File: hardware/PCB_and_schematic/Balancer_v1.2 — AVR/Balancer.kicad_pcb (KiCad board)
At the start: 2 copper layers, 99.5 x 99.5 mm, 189 parts, among them J1 BATT_OUT, J10 RS485, J11 HEATSING_TEMP1, J12 External Current Shunt, J13 BATT_IN, J2 VOLTAGE_3WIRE, J3 Conn_01x03, J4 HEATSING_TEMP1, J5 FAN1, J6 FAN2, J7 BATT_12V, J8 ICP, J9 RS485, Q1 BC817, Q10 TIP41C, Q11 TIP41C, Q12 BC807, Q13 BD238, Q14 TIP41C, Q15 BC807, Q16 BD238, Q17 BC817, Q19 BC817, Q2 BC337, Q20 BC817, Q21 BC817, Q22 BC817, Q23 TIP41C, Q3 BC327, Q4 PMOS, Q5 PMOS, Q6 BC337, Q7 BC327, Q8 BC817, Q9 BC817, U1 LM324, U2 LM324, U3 LM358, U4 TL432DBZ, U6 ST485, U7 INA226, U8 AVR64DD28

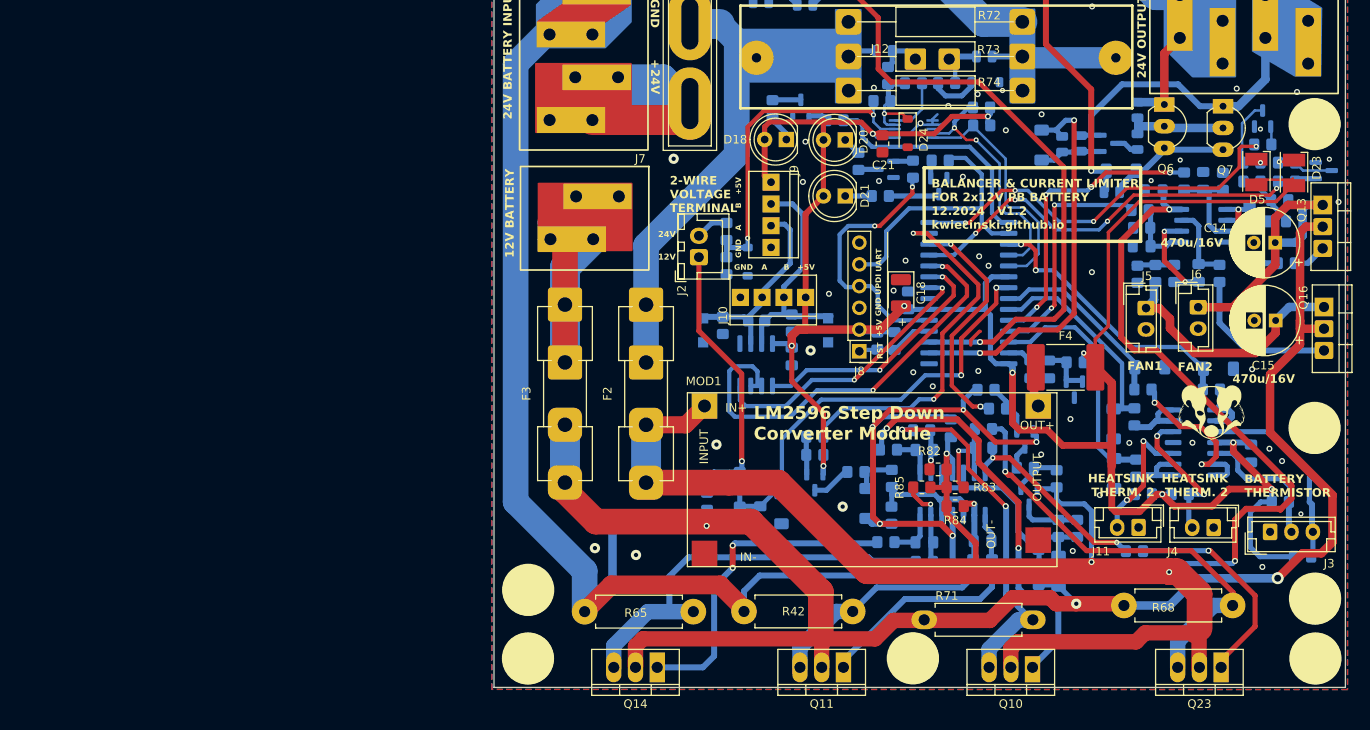
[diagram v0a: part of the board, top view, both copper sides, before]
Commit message: New version of balancer PCB and schematic
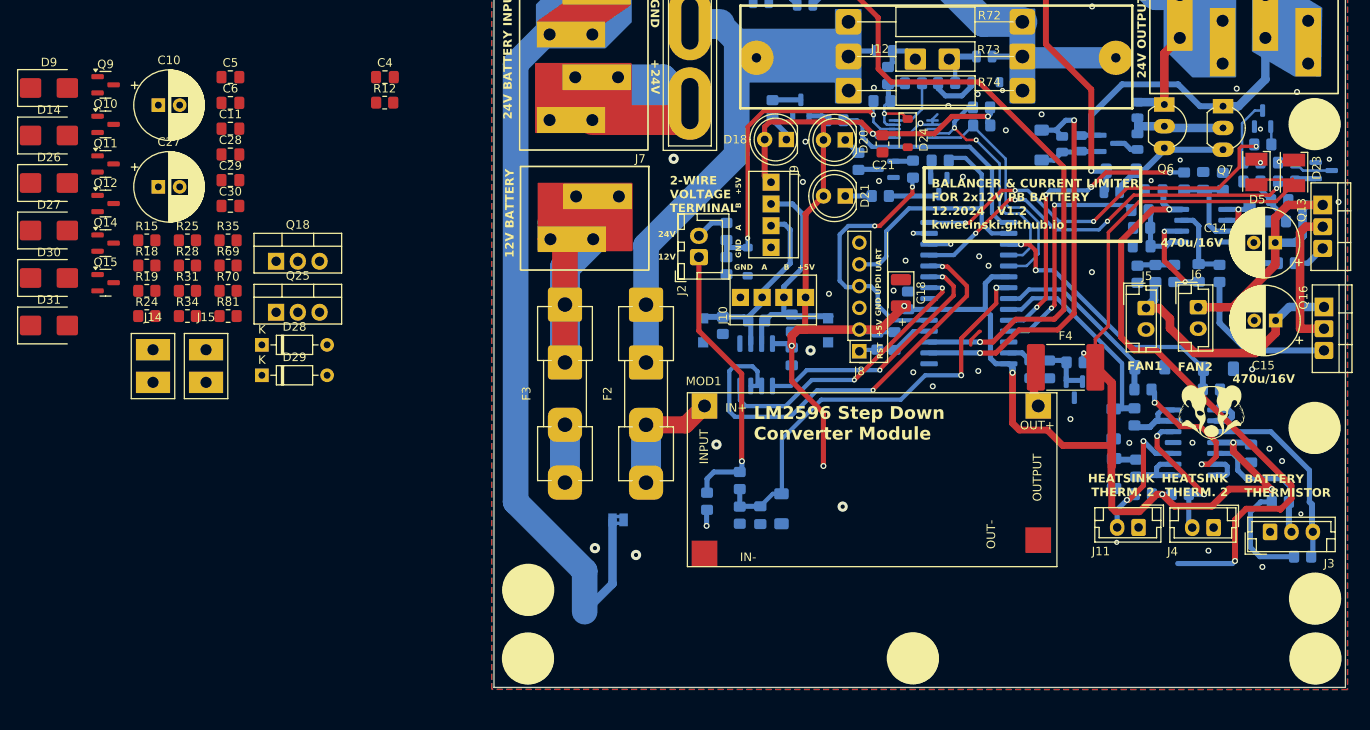
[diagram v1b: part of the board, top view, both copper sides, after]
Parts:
- removed Q23: TIP41C, My-Footprints:TO-220-3_V_Thick_Pads
- removed R36, R37, R86, R87, R88, R89: 1k, Resistor_SMD:R_0805_2012Metric_Pad1.20x1.40mm_HandSolder
- removed R42, R65, R68, R71: 0R1, My-Footprints:R_Axial_DIN0411_L9.9mm_D3.6mm_P12.70mm_Horizontal
- removed R82, R83, R84, R85: 1M, Resistor_SMD:R_0805_2012Metric_Pad1.20x1.40mm_HandSolder
- removed R90: 4k7, Resistor_SMD:R_0805_2012Metric_Pad1.20x1.40mm_HandSolder
- removed R91, R92, R93: 100k, Resistor_SMD:R_0805_2012Metric_Pad1.20x1.40mm_HandSolder
- removed U2: LM324, Package_SO:SOIC-14_3.9x8.7mm_P1.27mm
- added C27: 470u/25V, Capacitor_THT:CP_Radial_D8.0mm_P2.50mm, F.Cu at (117.8, 91.9)
- added C28: 10u, Capacitor_SMD:C_0805_2012Metric_Pad1.18x1.45mm_HandSolder, F.Cu at (126.2, 88.1)
- added C29: 100n, Capacitor_SMD:C_0805_2012Metric_Pad1.18x1.45mm_HandSolder, F.Cu at (126.2, 91.1)
- added C30: 1u, Capacitor_SMD:C_0805_2012Metric_Pad1.18x1.45mm_HandSolder, F.Cu at (126.2, 94.1)
- added D26: SM6T15A, Diode_SMD:D_SMB, F.Cu at (105.0, 91.4)
- added D27: SM6T15A, Diode_SMD:D_SMB, F.Cu at (105.0, 97.0)
- added D28: BAT86, Diode_THT:D_DO-35_SOD27_P7.62mm_Horizontal, F.Cu at (129.9, 110.3)
- added D29: BAT86, Diode_THT:D_DO-35_SOD27_P7.62mm_Horizontal, F.Cu at (129.9, 113.9)
- added D30: SM6T15A, Diode_SMD:D_SMB, F.Cu at (105.0, 102.5)
- added D31: SM6T15A, Diode_SMD:D_SMB, F.Cu at (105.0, 108.1)
- added J14: LOAD_RESISTOR, My-Footprints-connectors:Conn_1x2_wire, F.Cu at (117.2, 110.9)
- added J15: LOAD_RESISTOR, My-Footprints-connectors:Conn_1x2_wire, F.Cu at (123.4, 110.9)
- added Q18: IRF540N, Package_TO_SOT_THT:TO-220-3_Vertical, F.Cu at (131.5, 100.6)
- added Q25: IRF540N, Package_TO_SOT_THT:TO-220-3_Vertical, F.Cu at (131.5, 106.5)
- added R69: 2k2, Resistor_SMD:R_0805_2012Metric_Pad1.20x1.40mm_HandSolder, F.Cu at (125.9, 101.1)
- added R70: 10R, Resistor_SMD:R_0805_2012Metric_Pad1.20x1.40mm_HandSolder, F.Cu at (125.9, 104.0)
- C10: value 1n -> 470u/25V; footprint Capacitor_SMD:C_0805_2012Metric_Pad1.18x1.45mm_HandSolder -> Capacitor_THT:CP_Radial_D8.0mm_P2.50mm; moved to F.Cu
- C11: value 1n -> 1u; moved to F.Cu
- C17: value 100n -> 470n
- C4, Q9, R12, R25: moved to F.Cu
- C5: value 1n -> 100n; moved to F.Cu
- C6: value 1n -> 10u; moved to F.Cu
- D14, D9: value 3V3 -> SM6T15A; footprint Diode_SMD:D_MiniMELF -> Diode_SMD:D_SMB; moved to F.Cu
- Q10, Q14: value TIP41C -> BC807; footprint My-Footprints:TO-220-3_V_Thick_Pads -> Package_TO_SOT_SMD:SOT-23
- Q11: value TIP41C -> BC817; footprint My-Footprints:TO-220-3_V_Thick_Pads -> Package_TO_SOT_SMD:SOT-23
- Q12, Q15: value BC807 -> BC817; moved to F.Cu
- R15: value 2k2 -> 1k; moved to F.Cu
- R18: value 33k -> 1k; moved to F.Cu
- R19: value 2k2 -> 10k; moved to F.Cu
- R24: value 1k -> 10k; moved to F.Cu
- R28: value 4,7k -> 2k2; moved to F.Cu
- R31: value 120R -> 1k; moved to F.Cu
- R34, R35: value 120R -> 10R; moved to F.Cu
- R49: value 1k5 -> 1k
- R81: value 2k2 -> 10R; moved to F.Cu
- moved D9 130.8 mm to (105.0, 80.3), turned to 0 degrees
- moved Q10 125.5 mm to (111.6, 84.6), turned to 0 degrees
- moved Q9 115.2 mm to (111.6, 80.0), turned to 0 degrees
- moved R15 113.8 mm to (116.4, 98.1), turned to 0 degrees
- moved Q15 110.8 mm to (111.6, 103.1), turned to 0 degrees
- moved R19 109.4 mm to (116.4, 104.0), turned to 0 degrees
- moved R18 109.1 mm to (116.4, 101.1), turned to 0 degrees
- moved D14 104.8 mm to (105.0, 85.9), turned to 0 degrees
- moved Q11 104.4 mm to (111.6, 89.2), turned to 0 degrees
- moved C10 103.1 mm to (117.8, 82.3)
- moved C11 100.2 mm to (126.2, 85.1), turned to 0 degrees
- moved R81 100.1 mm to (125.9, 107.0), turned to 0 degrees
- moved R24 98.7 mm to (116.4, 107.0)
- moved C5 98.1 mm to (126.2, 79.1), turned to 0 degrees
- moved C6 90.7 mm to (126.2, 82.1)
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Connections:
- C10 pad 1: Net-(C10-Pad1) -> +BATT_12V
- C10 pad 2: Net-(U2D--) -> GNDA
- C4 pad 1: +BATT_24V -> +5V
- C4 pad 2: GNDA -> UPDI
- C5 pad 1: Net-(C5-Pad1) -> +BATT_12V
- C5 pad 2: Net-(U2B--) -> GNDA
- C6 pad 1: Net-(C6-Pad1) -> +BATT_12V
- C6 pad 2: Net-(U2A--) -> GNDA
- D14 pad 1: Net-(D14-K) -> BALANCE_ON_12V
- D9 pad 1: Net-(D9-K) -> BALANCE_ON_24V
- D9 pad 2: +BATT_12V -> GNDA
- Q10 pad 2: +BATT_24V -> Net-(Q10-E)
- Q10 pad 3: Net-(Q10-E) -> +BATT_12V
- Q11 pad 2: +BATT_12V -> Net-(Q11-E)
- Q11 pad 3: Net-(Q11-E) -> Net-(Q11-C)
- Q12 pad 1: Net-(Q12-B) -> Net-(Q11-C)
- Q12 pad 2: +5V -> Net-(Q12-E)
- Q12 pad 3: Net-(Q12-C) -> +BATT_12V
- Q14 pad 1: Net-(Q14-B) -> Net-(Q11-C)
- Q14 pad 2: +BATT_12V -> Net-(Q12-E)
- Q14 pad 3: Net-(Q14-E) -> GNDA
- Q15 pad 2: +BATT_24V -> Net-(Q15-E)
- Q15 pad 3: Net-(Q15-C) -> Net-(Q10-B)
- Q9 pad 1: Net-(Q9-B) -> Net-(Q10-B)
- Q9 pad 2: GNDA -> Net-(Q10-E)
- Q9 pad 3: Net-(Q9-C) -> +BATT_24V
- R12 pad 1: Net-(Q9-B) -> +5V
- R12 pad 2: BALANCE_ON_24V -> UPDI
- R15 pad 1: Net-(D9-K) -> Net-(Q15-B)
- R15 pad 2: Net-(Q15-C) -> BALANCE_ON_24V
- R18 pad 1: Net-(U2A-+) -> Net-(Q15-E)
- R18 pad 2: Net-(D9-K) -> GNDA
- R19 pad 1: +BATT_12V -> +5V
- R19 pad 2: Net-(U2A-+) -> BALANCE_ON_24V
- R24 pad 1: Net-(U2B--) -> +5V
- R24 pad 2: Net-(Q23-E) -> BALANCE_ON_12V
- R25 pad 1: Net-(U2A--) -> Net-(Q11-B)
- R25 pad 2: Net-(Q10-E) -> BALANCE_ON_12V
- R28 pad 1: Net-(Q12-B) -> +BATT_12V
- R28 pad 2: BALANCE_ON_12V -> Net-(Q11-C)
- R31 pad 1: Net-(D14-K) -> Net-(Q11-E)
- R31 pad 2: Net-(Q12-C) -> GNDA
- R34 pad 1: Net-(U2C-+) -> Net-(D29-K)
- R34 pad 2: Net-(D14-K) -> Net-(Q12-E)
- R35 pad 1: GNDA -> Net-(D31-A1)
- R35 pad 2: Net-(U2C-+) -> Net-(C11-Pad1)
- R81 pad 1: Net-(Q15-C) -> Net-(D26-A1)
- R81 pad 2: Net-(D9-K) -> Net-(C30-Pad1)
- U8 pad 12: TEMP_HEAT_SINK_12V -> DAC
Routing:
- net +BATT_12V: track 195.6 -> 25.6 mm, vias 3 -> 1
- net +BATT_24V: track 224.3 -> 85.1 mm, vias 5 -> 2
- net GNDA: track 278.4 -> 163.8 mm, vias 7 -> 2
- net Net-(Q23-E): track 51.9 -> 0.00 mm, vias 1 -> 0
- net Net-(Q14-E): track 50.1 -> 0.00 mm
- net Net-(Q10-B): track 47.7 -> 0.00 mm, vias 2 -> 0
- net Net-(Q10-E): track 41.3 -> 0.00 mm, vias 2 -> 0
- net BALANCE_ON_12V: track 41.8 -> 0.79 mm, vias 2 -> 1
- net Net-(Q14-B): track 38.1 -> 0.00 mm, vias 2 -> 0
- net Net-(Q11-E): track 26.2 -> 0.00 mm
- net TEMP_HEAT_SINK_12V: track 28.6 -> 2.63 mm
- net BALANCE_ON_24V: track 27.9 -> 2.53 mm, vias 2 -> 1
- net Net-(Q23-B): track 25.3 -> 0.00 mm, vias 1 -> 0
- net Net-(C5-Pad1): track 23.4 -> 0.00 mm, vias 2 -> 0
- net Net-(Q11-B): track 23.1 -> 0.00 mm
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
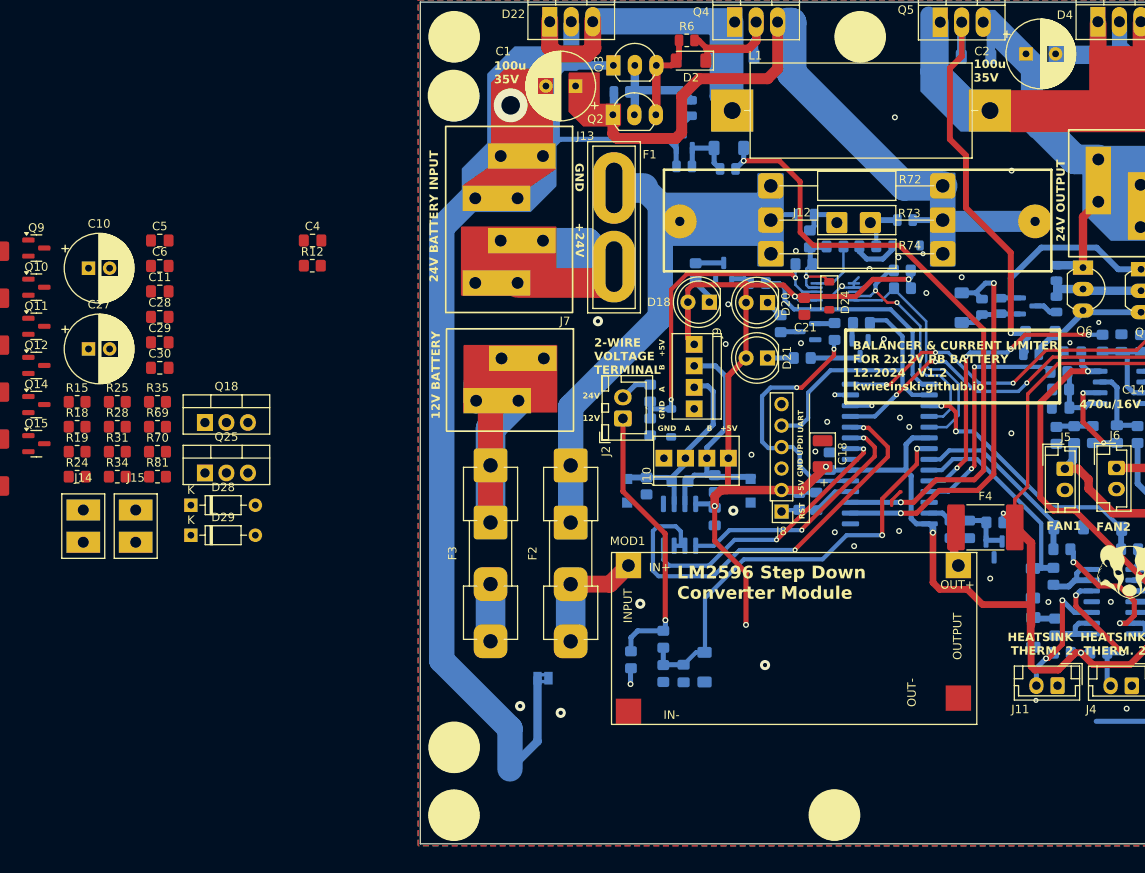
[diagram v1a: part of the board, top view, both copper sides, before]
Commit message: Update electrical schematic and BMS schematic
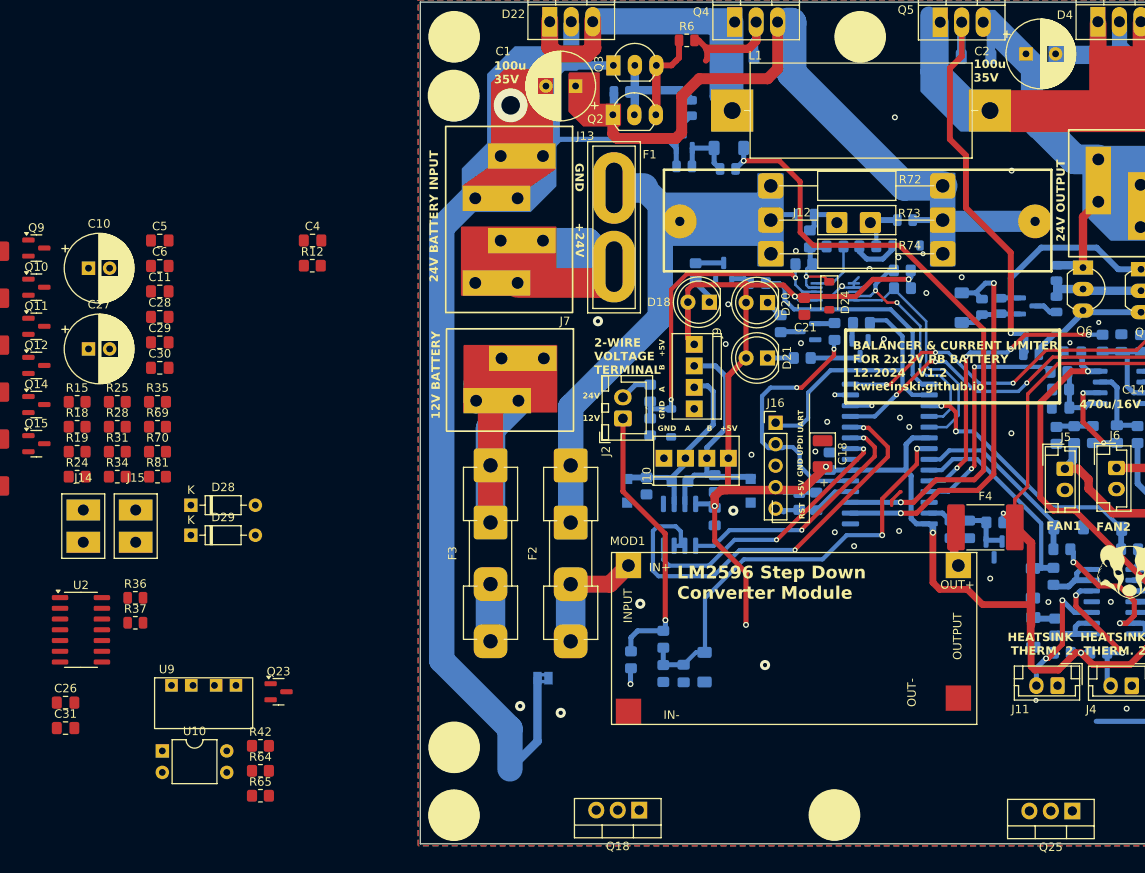
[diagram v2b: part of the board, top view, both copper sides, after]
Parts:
- removed D2, D7: LL4148, Diode_SMD:D_MiniMELF
- removed J8: ICP, Connector_PinHeader_2.54mm:PinHeader_1x06_P2.54mm_Vertical
- added C26: 1u, Capacitor_SMD:C_0805_2012Metric_Pad1.18x1.45mm_HandSolder, F.Cu at (115.1, 133.7)
- added C31: 100n, Capacitor_SMD:C_0805_2012Metric_Pad1.18x1.45mm_HandSolder, F.Cu at (115.1, 136.7)
- added J16: ICP, Connector_PinHeader_2.54mm:PinHeader_1x05_P2.54mm_Vertical, F.Cu at (199.0, 100.6)
- added Q23: BC817, Package_TO_SOT_SMD:SOT-23, F.Cu at (140.2, 132.4)
- added R36: 10k, Resistor_SMD:R_0805_2012Metric, F.Cu at (123.3, 121.3)
- added R37: 10k, Resistor_SMD:R_0805_2012Metric, F.Cu at (123.3, 124.2)
- added R42: 1k, Resistor_SMD:R_0805_2012Metric_Pad1.20x1.40mm_HandSolder, F.Cu at (138.1, 138.8)
- added R64: 1k, Resistor_SMD:R_0805_2012Metric_Pad1.20x1.40mm_HandSolder, F.Cu at (138.1, 141.8)
- added R65: 4k7, Resistor_SMD:R_0805_2012Metric_Pad1.20x1.40mm_HandSolder, F.Cu at (138.1, 144.7)
- added U10: PC817, Package_DIP:DIP-4_W7.62mm, F.Cu at (126.5, 139.4)
- added U2: 74AHCT125, Package_SO:SOIC-14_3.9x8.7mm_P1.27mm, F.Cu at (116.9, 125.1)
- added U9: B0505S-1W, My-Footprints:B0505S, F.Cu at (125.6, 130.8)
- R6: value 1k -> 10R
- R7: value 100R -> 10R
- moved Q25 110.1 mm to (234.1, 146.5), turned to 180 degrees
- moved Q18 68.8 mm to (182.9, 146.4), turned to 180 degrees
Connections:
- C20 pad 2: GND -> GND_RS485
- D1 pad 1: PWM_OUT_DISCH -> Net-(D1-K)
- D14 pad 1: BALANCE_ON_12V -> Net-(D14-A1)
- D16 pad 1: GND -> GND_RS485
- D17 pad 1: GND -> GND_RS485
- D8 pad 1: PWM_OUT_CHRG -> Net-(D8-K)
- D9 pad 1: BALANCE_ON_24V -> Net-(D9-A1)
- J10 pad 1: +5V -> +5V_RS485
- J10 pad 4: GND -> GND_RS485
- J9 pad 1: +5V -> +5V_RS485
- J9 pad 4: GND -> GND_RS485
- R1 pad 1: PWM_OUT_DISCH -> Net-(D1-K)
- R11 pad 1: PWM_OUT_CHRG -> Net-(D8-K)
- R15 pad 2: BALANCE_ON_24V -> Net-(D9-A1)
- R25 pad 2: BALANCE_ON_12V -> Net-(D14-A1)
- R51 pad 1: +5V -> +5V_RS485
- R53 pad 2: GND -> GND_RS485
- U6 pad 1: RS232_RX -> Net-(U5-VIA)
- U6 pad 2: RS485_OUTPUT_ENABLE -> Net-(U6-DE)
- U6 pad 3: RS485_OUTPUT_ENABLE -> Net-(U6-DE)
- U6 pad 4: RS232_TX -> Net-(U5-VOB)
- U6 pad 5: GND -> GND_RS485
- U6 pad 8: +5V -> +5V_RS485

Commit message: Balancer PCB update
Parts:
- added C32: 100n, Capacitor_SMD:C_0805_2012Metric_Pad1.18x1.45mm_HandSolder, B.Cu at (190.3, 108.7)
- added D2: BAT86, Diode_SMD:D_MiniMELF, F.Cu at (213.4, 120.4)
- added D7: BAT86, Diode_SMD:D_MiniMELF, F.Cu at (95.5, 147.6)
- added U5: ADUM3211ARZ, Package_SO:SO-8_3.9x4.9mm_P1.27mm, B.Cu at (195.6, 109.4)
- C28, C29, C30, D26, D27, Q10, Q15, Q23, Q9, R15, R19, R42, R64, R65, R70, R81, U2: moved to B.Cu
- D14, D9: value SM6T15A -> BAT86; footprint Diode_SMD:D_SMB -> Diode_SMD:D_MiniMELF
- D28: footprint Diode_THT:D_DO-35_SOD27_P7.62mm_Horizontal -> Diode_SMD:D_MiniMELF; moved to B.Cu
- R18: value 1k -> 470R; moved to B.Cu
- R28: footprint Resistor_SMD:R_0805_2012Metric_Pad1.20x1.40mm_HandSolder -> Resistor_SMD:R_1206_3216Metric_Pad1.30x1.75mm_HandSolder
- R31: value 1k -> 220R
- R69: footprint Resistor_SMD:R_0805_2012Metric_Pad1.20x1.40mm_HandSolder -> Resistor_SMD:R_1206_3216Metric_Pad1.30x1.75mm_HandSolder; moved to B.Cu
- moved D27 132.2 mm to (228.1, 145.4), turned to 90 degrees
- moved J14 128.8 mm to (240.7, 147.3), turned to -90 degrees
- moved D20 125.9 mm to (86.0, 29.0)
- moved D21 125.9 mm to (86.0, 35.5)
- moved Q17 125.9 mm to (80.9, 25.2)
- moved Q20 125.9 mm to (97.0, 34.4)
- moved R57 125.9 mm to (77.5, 25.4)
- moved R60 125.9 mm to (94.0, 32.4)
- moved D18 125.9 mm to (79.2, 28.9)
- moved D23 125.9 mm to (138.5, 32.9)
- moved D5 125.9 mm to (134.1, 32.8)
- moved Q19 125.9 mm to (90.8, 32.4)
- moved Q21 125.9 mm to (134.8, 26.5)
- moved Q22 125.9 mm to (142.0, 32.6)
- moved R56 125.9 mm to (84.8, 26.7)
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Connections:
- C20 pad 1: +5V -> +5V_RS485
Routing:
- net +5V: track 268.7 -> 157.3 mm, vias 10 -> 6
- net PWM_OUT_DISCH: track 77.0 -> 0.00 mm, vias 2 -> 0
- net Net-(D1-K): track 0.00 -> 71.0 mm, vias 0 -> 1
- net +5V_RS485: track 0.00 -> 52.0 mm, vias 0 -> 3
- net GND_RS485: track 0.00 -> 48.0 mm
- net RS485_OUTPUT_ENABLE: track 51.9 -> 5.10 mm, vias 2 -> 0
- net PWM_OUT_CHRG: track 46.6 -> 0.00 mm, vias 2 -> 0
- net VOLTAGE_BATT_12V: track 51.4 -> 9.08 mm, vias 2 -> 1
- net Net-(D8-K): track 0.00 -> 40.8 mm, vias 0 -> 1
- net Net-(D25-K): track 39.5 -> 0.00 mm, vias 2 -> 0
- net RS232_TX: track 33.2 -> 0.00 mm, vias 2 -> 0
- net Net-(J2-Pin_1): track 33.1 -> 0.00 mm, vias 1 -> 0
- net UPDI: track 31.2 -> 0.00 mm, vias 2 -> 0
- net DBG_UART: track 32.6 -> 1.99 mm
- net RS232_RX: track 29.9 -> 0.00 mm, vias 2 -> 0
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- added copper zone on B.Cu, net GND_RS485
- added copper zone on F.Cu, net GND_RS485
